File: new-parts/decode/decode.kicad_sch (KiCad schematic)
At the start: 45 parts, among them J1 BHR-10-VUA, J10 Conn_01x01, J11 Conn_01x01, J12 Conn_01x01, J13 Conn_01x01, J14 Conn_01x01, J2 Conn_01x01, J3 Conn_01x01, J4 Conn_01x01, J5 Conn_01x01, J6 Conn_01x03, J7 Conn_01x01, J8 Conn_01x01, J9 Conn_01x01, K1 J104D2C12VDC.15S, K2 J104D2C12VDC.15S, K3 J104D2C12VDC.15S, K4 J104D2C12VDC.15S, K5 J104D2C12VDC.15S, K6 J104D2C12VDC.15S, K7 J104D2C12VDC.15S, K8 J104D2C12VDC.15S, K9 J104D2C12VDC.15S

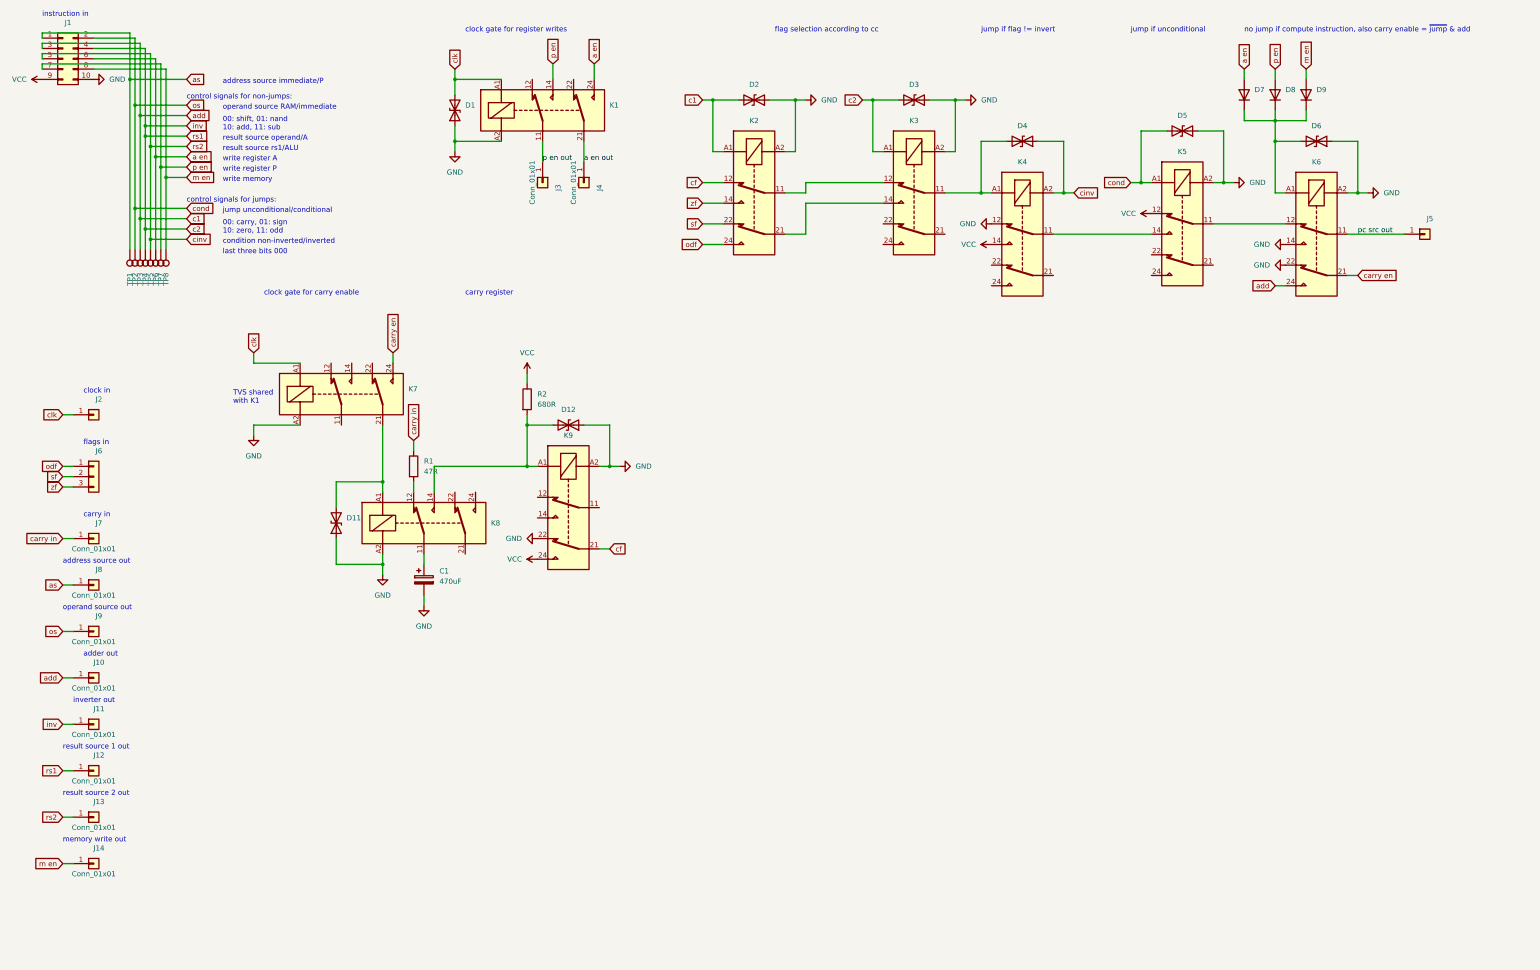
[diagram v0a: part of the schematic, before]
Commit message: decode: Also provide !invert control signal as carry in for the adder, provide 4 pins for every control signal.
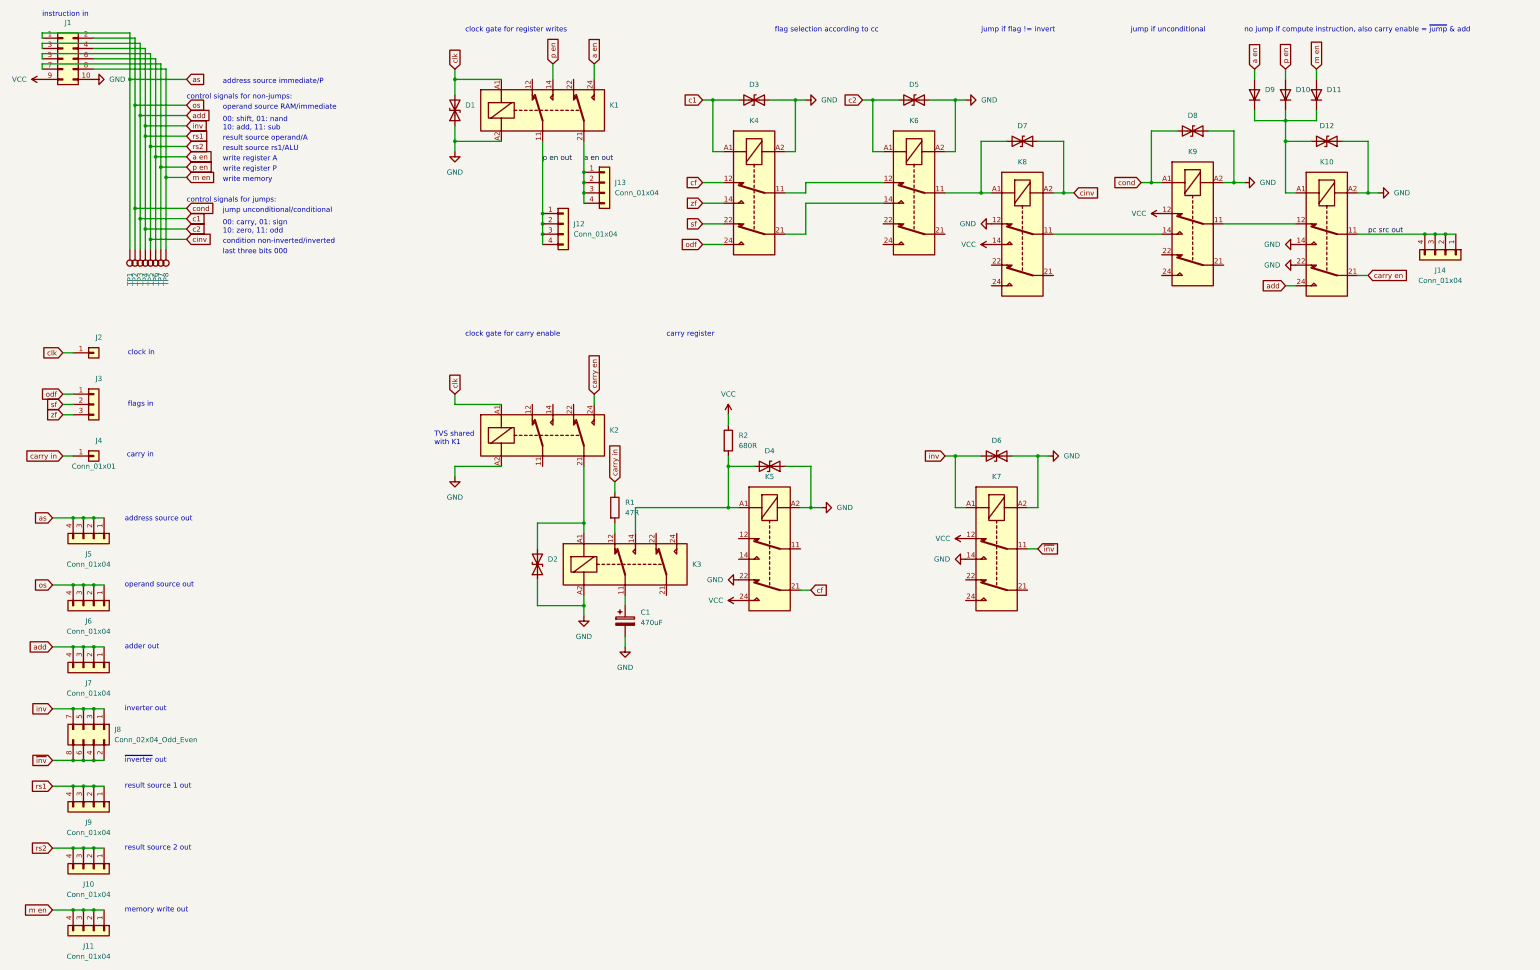
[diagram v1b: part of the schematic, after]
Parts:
- removed J10, J11, J12, J13, J14, J3, J4, J5, J8, J9: Conn_01x01, Connector_PinHeader_2.54mm:PinHeader_1x01_P2.54mm_Vertical, symbol Connector_Generic:Conn_01x01
- added D6: SMAJ14CA, Diode_SMD:D_SMA_Handsoldering, symbol Device:D_TVS
- added J10, J11, J12, J13, J14, J5, J6, J7, J9: Conn_01x04, Connector_PinHeader_2.54mm:PinHeader_1x04_P2.54mm_Vertical, symbol Connector_Generic:Conn_01x04
- added J8: Conn_02x04_Odd_Even, Connector_PinHeader_2.54mm:PinHeader_2x04_P2.54mm_Vertical, symbol Connector_Generic:Conn_02x04_Odd_Even
- added K7: J104D2C12VDC.15S, Relay_THT:Relay_DPDT_Finder_30.22, symbol Relay:Relay_DPDT
- renumbered D8 to D10, D9 to D11, D6 to D12, D11 to D2, D2 to D3, D12 to D4, D3 to D5, D4 to D7, D5 to D8, D7 to D9, J6 to J3, J7 to J4, K6 to K10, K7 to K2, K8 to K3, K2 to K4, K9 to K5, K3 to K6, K4 to K8, K5 to K9
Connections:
- net GND: now also D6.1 (A1), K7.14, K7.A2
- net VCC: now also K7.12
- net a en out: now also J13.1 (Pin_1), J13.2 (Pin_2), J13.3 (Pin_3), J13.4 (Pin_4)
- net add: now also J7.1 (Pin_1), J7.2 (Pin_2), J7.3 (Pin_3), J7.4 (Pin_4)
- net as: now also J5.1 (Pin_1), J5.2 (Pin_2), J5.3 (Pin_3), J5.4 (Pin_4)
- net c2: now also D6.2 (A2), J8.1 (Pin_1), J8.3 (Pin_3), J8.5 (Pin_5), J8.7 (Pin_7), J9.1 (Pin_1), J9.2 (Pin_2), J9.3 (Pin_3), J9.4 (Pin_4), K7.A1
- net cinv: now also J10.1 (Pin_1), J10.2 (Pin_2), J10.3 (Pin_3), J10.4 (Pin_4)
- net cond: now also J6.1 (Pin_1), J6.2 (Pin_2), J6.3 (Pin_3), J6.4 (Pin_4)
- net m en: now also J11.1 (Pin_1), J11.2 (Pin_2), J11.3 (Pin_3), J11.4 (Pin_4)
- net p en out: now also J12.1 (Pin_1), J12.2 (Pin_2), J12.3 (Pin_3), J12.4 (Pin_4)
- net pc src out: now also J14.1 (Pin_1), J14.2 (Pin_2), J14.3 (Pin_3), J14.4 (Pin_4)
- new net ~{inv}: J8.2 (Pin_2), J8.4 (Pin_4), J8.6 (Pin_6), J8.8 (Pin_8), K7.11
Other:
- note added: "~{inverter} out"
- moved on the sheet: C1, D10, D11, D12, D2, D4, D8, D9, J2, J3, J4, K10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
